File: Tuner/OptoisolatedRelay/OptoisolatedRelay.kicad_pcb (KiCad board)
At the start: 2 copper layers, 100 x 100 mm, 94 parts, among them J1 Conn_02x05_Odd_Even, J10 Conn_01x02, J11 Conn_01x02, J12 Conn_01x01, J13 Conn_01x01, J14 Conn_01x02, J15 Conn_01x02, J16 Conn_01x02, J17 Conn_01x02, J18 Conn_01x02, J19 Conn_01x02, J2 Conn_01x02, J20 Conn_01x02, J21 Conn_01x02, J22 Conn_01x02, J3 Conn_01x01, J4 Conn_01x01, J5 Conn_01x02, J6 Conn_01x02, J7 Conn_01x02, J8 Conn_01x02, J9 Conn_01x02, U1 MCP23017, U10 PC817, U11 PC817, U12 PC817, U13 PC817, U14 PC817, U15 PC817, U16 PC817, U17 PC817, U18 PC817, U19 PC817, U2 ULN2803A, U3 ULN2803A, U4 PC817, U5 PC817, U6 PC817, U7 PC817, U8 PC817, U9 PC817

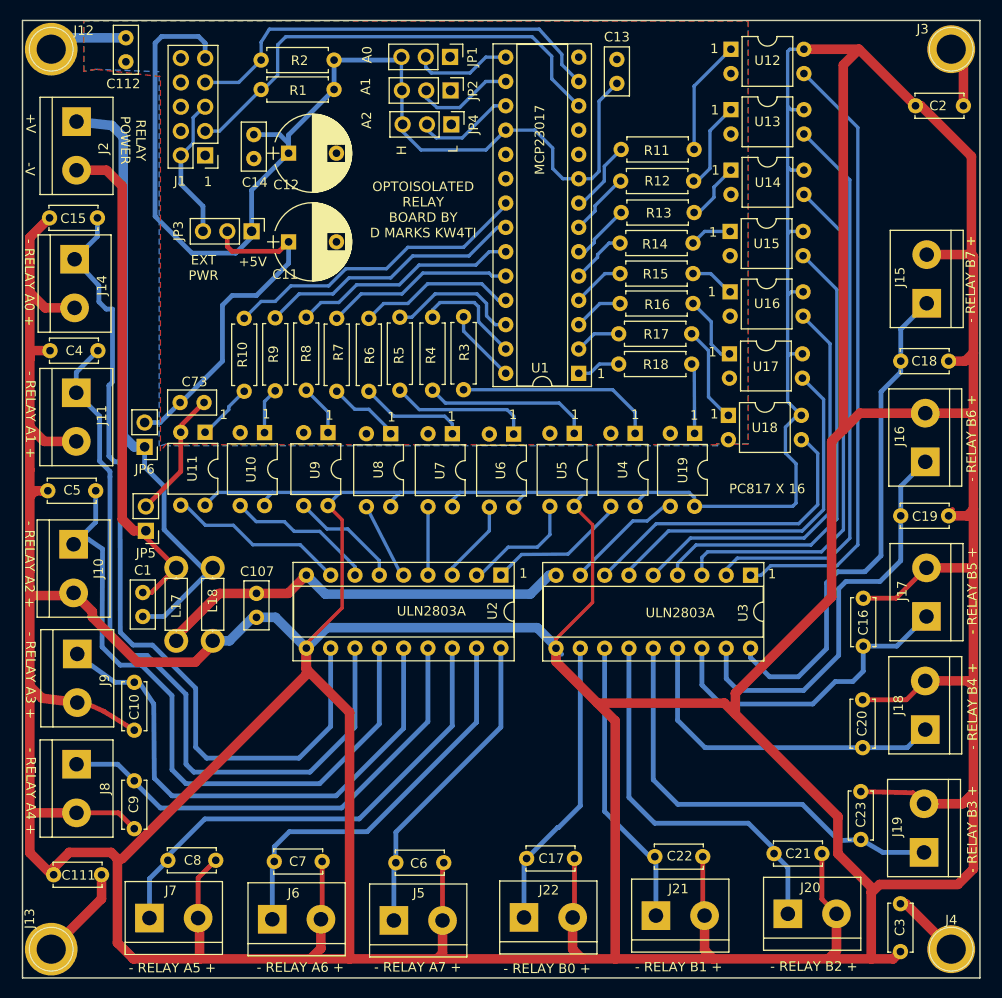
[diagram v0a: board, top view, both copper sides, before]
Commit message: Added LEDs to OptoisolatedRelay
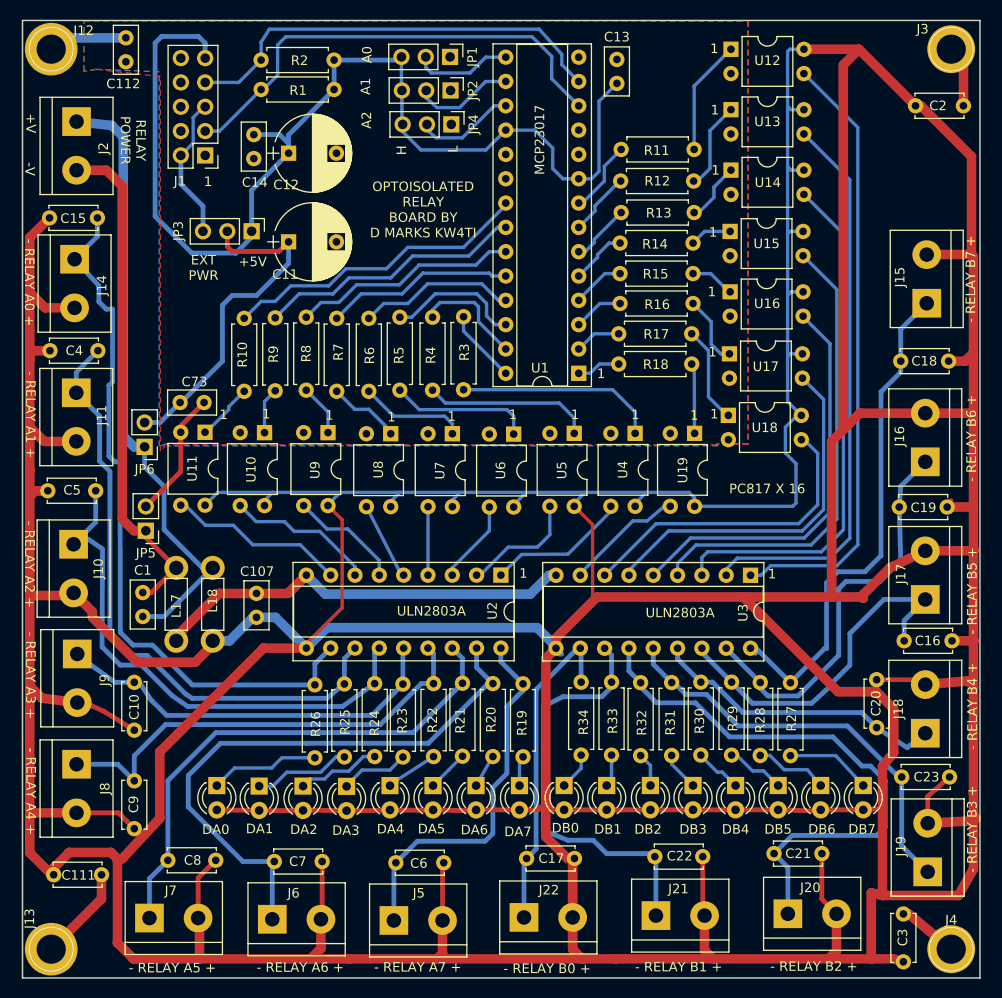
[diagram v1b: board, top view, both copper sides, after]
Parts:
- added DA0: LED, LEDs:LED_D3.0mm, F.Cu at (71.3, 128.9)
- added DA1: LED, LEDs:LED_D3.0mm, F.Cu at (75.7, 129.0)
- added DA2: LED, LEDs:LED_D3.0mm, F.Cu at (80.3, 129.0)
- added DA3: LED, LEDs:LED_D3.0mm, F.Cu at (84.8, 129.0)
- added DA4: LED, LEDs:LED_D3.0mm, F.Cu at (89.4, 128.9)
- added DA5: LED, LEDs:LED_D3.0mm, F.Cu at (93.9, 128.9)
- added DA6: LED, LEDs:LED_D3.0mm, F.Cu at (98.4, 128.9)
- added DA7: LED, LEDs:LED_D3.0mm, F.Cu at (102.9, 128.9)
- added DB0: LED, LEDs:LED_D3.0mm, F.Cu at (107.6, 128.9)
- added DB1: LED, LEDs:LED_D3.0mm, F.Cu at (112.0, 128.9)
- added DB2: LED, LEDs:LED_D3.0mm, F.Cu at (116.6, 128.9)
- added DB3: LED, LEDs:LED_D3.0mm, F.Cu at (121.0, 128.9)
- added DB4: LED, LEDs:LED_D3.0mm, F.Cu at (125.5, 128.9)
- added DB5: LED, LEDs:LED_D3.0mm, F.Cu at (129.9, 128.9)
- added DB6: LED, LEDs:LED_D3.0mm, F.Cu at (134.4, 128.9)
- added DB7: LED, LEDs:LED_D3.0mm, F.Cu at (138.8, 128.9)
- added R19: 1k, Resistors_THT:R_Axial_DIN0207_L6.3mm_D2.5mm_P7.62mm_Horizontal, F.Cu at (103.3, 125.9)
- added R20: 1k, Resistors_THT:R_Axial_DIN0207_L6.3mm_D2.5mm_P7.62mm_Horizontal, F.Cu at (100.1, 125.9)
- added R21: 1k, Resistors_THT:R_Axial_DIN0207_L6.3mm_D2.5mm_P7.62mm_Horizontal, F.Cu at (97.0, 125.8)
- added R22: 1k, Resistors_THT:R_Axial_DIN0207_L6.3mm_D2.5mm_P7.62mm_Horizontal, F.Cu at (93.9, 125.9)
- added R23: 1k, Resistors_THT:R_Axial_DIN0207_L6.3mm_D2.5mm_P7.62mm_Horizontal, F.Cu at (90.7, 125.9)
- added R24: 1k, Resistors_THT:R_Axial_DIN0207_L6.3mm_D2.5mm_P7.62mm_Horizontal, F.Cu at (87.8, 125.9)
- added R25: 1k, Resistors_THT:R_Axial_DIN0207_L6.3mm_D2.5mm_P7.62mm_Horizontal, F.Cu at (84.6, 125.9)
- added R26: 1k, Resistors_THT:R_Axial_DIN0207_L6.3mm_D2.5mm_P7.62mm_Horizontal, F.Cu at (81.5, 126.0)
- added R27: 1k, Resistors_THT:R_Axial_DIN0207_L6.3mm_D2.5mm_P7.62mm_Horizontal, F.Cu at (131.2, 125.8)
- added R28: 1k, Resistors_THT:R_Axial_DIN0207_L6.3mm_D2.5mm_P7.62mm_Horizontal, F.Cu at (128.1, 125.8)
- added R29: 1k, Resistors_THT:R_Axial_DIN0207_L6.3mm_D2.5mm_P7.62mm_Horizontal, F.Cu at (125.1, 125.7)
- added R30: 1k, Resistors_THT:R_Axial_DIN0207_L6.3mm_D2.5mm_P7.62mm_Horizontal, F.Cu at (121.8, 125.7)
- added R31: 1k, Resistors_THT:R_Axial_DIN0207_L6.3mm_D2.5mm_P7.62mm_Horizontal, F.Cu at (118.8, 125.8)
- added R32: 1k, Resistors_THT:R_Axial_DIN0207_L6.3mm_D2.5mm_P7.62mm_Horizontal, F.Cu at (115.6, 125.8)
- added R33: 1k, Resistors_THT:R_Axial_DIN0207_L6.3mm_D2.5mm_P7.62mm_Horizontal, F.Cu at (112.5, 125.7)
- added R34: 1k, Resistors_THT:R_Axial_DIN0207_L6.3mm_D2.5mm_P7.62mm_Horizontal, F.Cu at (109.3, 125.7)
- moved C16 10.3 mm to (148.1, 113.8), turned to 180 degrees
- moved C23 9.40 mm to (147.8, 128.0), turned to 180 degrees
- moved C20 2.55 mm to (140.2, 117.9)
- moved J19 2.07 mm to (145.5, 137.9)
- moved J17 1.78 mm to (145.3, 109.5)
- moved C3 1.11 mm to (143.0, 147.3)
- moved C19 0.93 mm to (147.6, 99.8)
- moved J18 0.38 mm to (145.3, 123.4)
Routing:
- net RLYPWR: track 909.0 -> 957.6 mm
- net Net-(C7-Pad2): track 41.9 -> 60.9 mm
- net Net-(C21-Pad2): track 40.3 -> 59.1 mm
- net Net-(C5-Pad2): track 73.3 -> 58.9 mm
- net Net-(C10-Pad2): track 56.1 -> 41.9 mm
- net Net-(C4-Pad2): track 80.8 -> 66.7 mm
- net Net-(C22-Pad2): track 30.5 -> 44.4 mm
- net Net-(C15-Pad2): track 87.8 -> 74.8 mm
- net Net-(DA0-Pad1): track 0.00 -> 11.7 mm
- net Net-(DA1-Pad1): track 0.00 -> 10.5 mm
- net Net-(DA2-Pad1): track 0.00 -> 9.48 mm
- net Net-(DB7-Pad1): track 0.00 -> 8.97 mm
- net Net-(DB6-Pad1): track 0.00 -> 7.69 mm
- net Net-(DA3-Pad1): track 0.00 -> 7.26 mm
- net Net-(C6-Pad2): track 33.1 -> 39.9 mm
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
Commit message: Added some fixes to tuner code
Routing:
- net +5V: track 114.7 -> 114.0 mm
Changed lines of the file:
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@@
   )
   (setup
-    (last_trace_width 1)
+    (last_trace_width 0.25)
     (user_trace_width 0.35)
     (user_trace_width 0.5)
@@
     (effects (font (size 1 1) (thickness 0.15)))
   )
-  (gr_text "- RELAY B6 +" (at 150.114 92.6338 90) (layer F.SilkS)
+  (gr_text "- RELAY B6 +" (at 150.241 92.456 90) (layer F.SilkS)
     (effects (font (size 1 1) (thickness 0.15)))
   )
-  (gr_text "- RELAY B5 +" (at 150.1902 108.5596 90) (layer F.SilkS)
+  (gr_text "- RELAY B5 +" (at 150.114 106.934 90) (layer F.SilkS)
     (effects (font (size 1 1) (thickness 0.15)))
   )
@@
     (effects (font (size 1 1) (thickness 0.15)))
   )
-  (gr_text "- RELAY B3 +" (at 150.1902 133.4516 90) (layer F.SilkS)
+  (gr_text "- RELAY B3 +" (at 150.241 135.255 90) (layer F.SilkS)
     (effects (font (size 1 1) (thickness 0.15)))
   )
@@
   (segment (start 74.93 71.6407) (end 73.2663 73.3044) (width 0.5) (layer B.Cu) (net 2) (status 10))
   (segment (start 73.2663 73.3044) (end 68.6943 73.3044) (width 0.5) (layer B.Cu) (net 2))
-  (segment (start 68.6943 73.3044) (end 64.8462 69.4563) (width 0.5) (layer B.Cu) (net 2))
-  (segment (start 64.8462 69.4563) (end 64.8462 51.3588) (width 0.5) (layer B.Cu) (net 2))
-  (segment (start 64.8462 51.3588) (end 65.532 50.673) (width 0.5) (layer B.Cu) (net 2))
+  (segment (start 68.6943 73.3044) (end 65.6082 69.4563) (width 0.5) (layer B.Cu) (net 2))
+  (segment (start 65.6082 69.4563) (end 65.6082 51.3588) (width 0.5) (layer B.Cu) (net 2))
+  (segment (start 65.6082 51.3588) (end 65.532 50.673) (width 0.5) (layer B.Cu) (net 2))
   (segment (start 65.532 50.673) (end 69.3801 50.673) (width 0.5) (layer B.Cu) (net 2))
   (segment (start 69.3801 50.673) (end 70.0786 51.3715) (width 0.5) (layer B.Cu) (net 2))
